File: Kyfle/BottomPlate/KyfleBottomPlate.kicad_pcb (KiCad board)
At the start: 2 copper layers, 161.3 x 139.1 mm, 52 parts, among them SW2 KEY_SWITCH, SW2 PRO MICRO

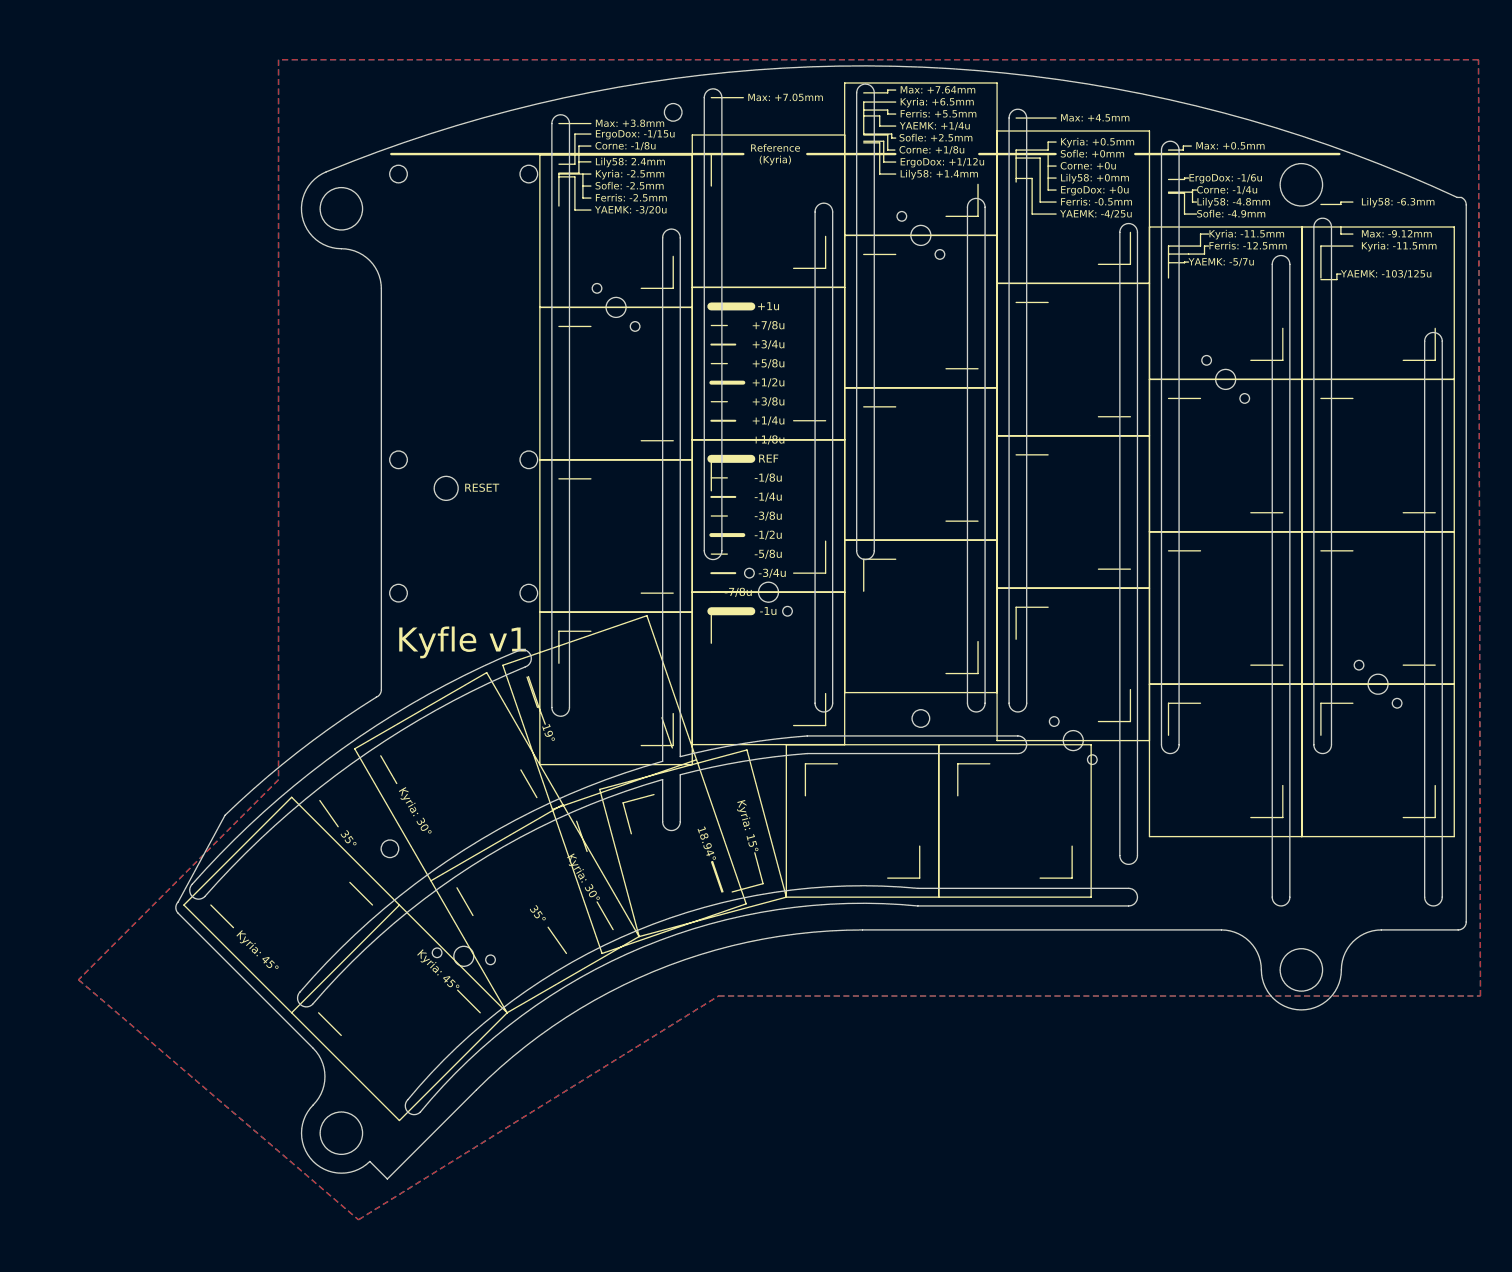
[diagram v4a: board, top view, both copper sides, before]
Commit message: Plates outlines finished
Redefined the various outlines of the plates based on the new constrains.
For the top dimension, I took the largest middle-finger stagerring I could find (Elephant42, at +9.5mm) and rounded it to 10mm max amplitude in the middle finger rail, and used that as reference for the position of the top arc (giving 3mm margin above that highest slot).
And defined the position of the rest from that.
Top left M% hole might need to be reviewed.
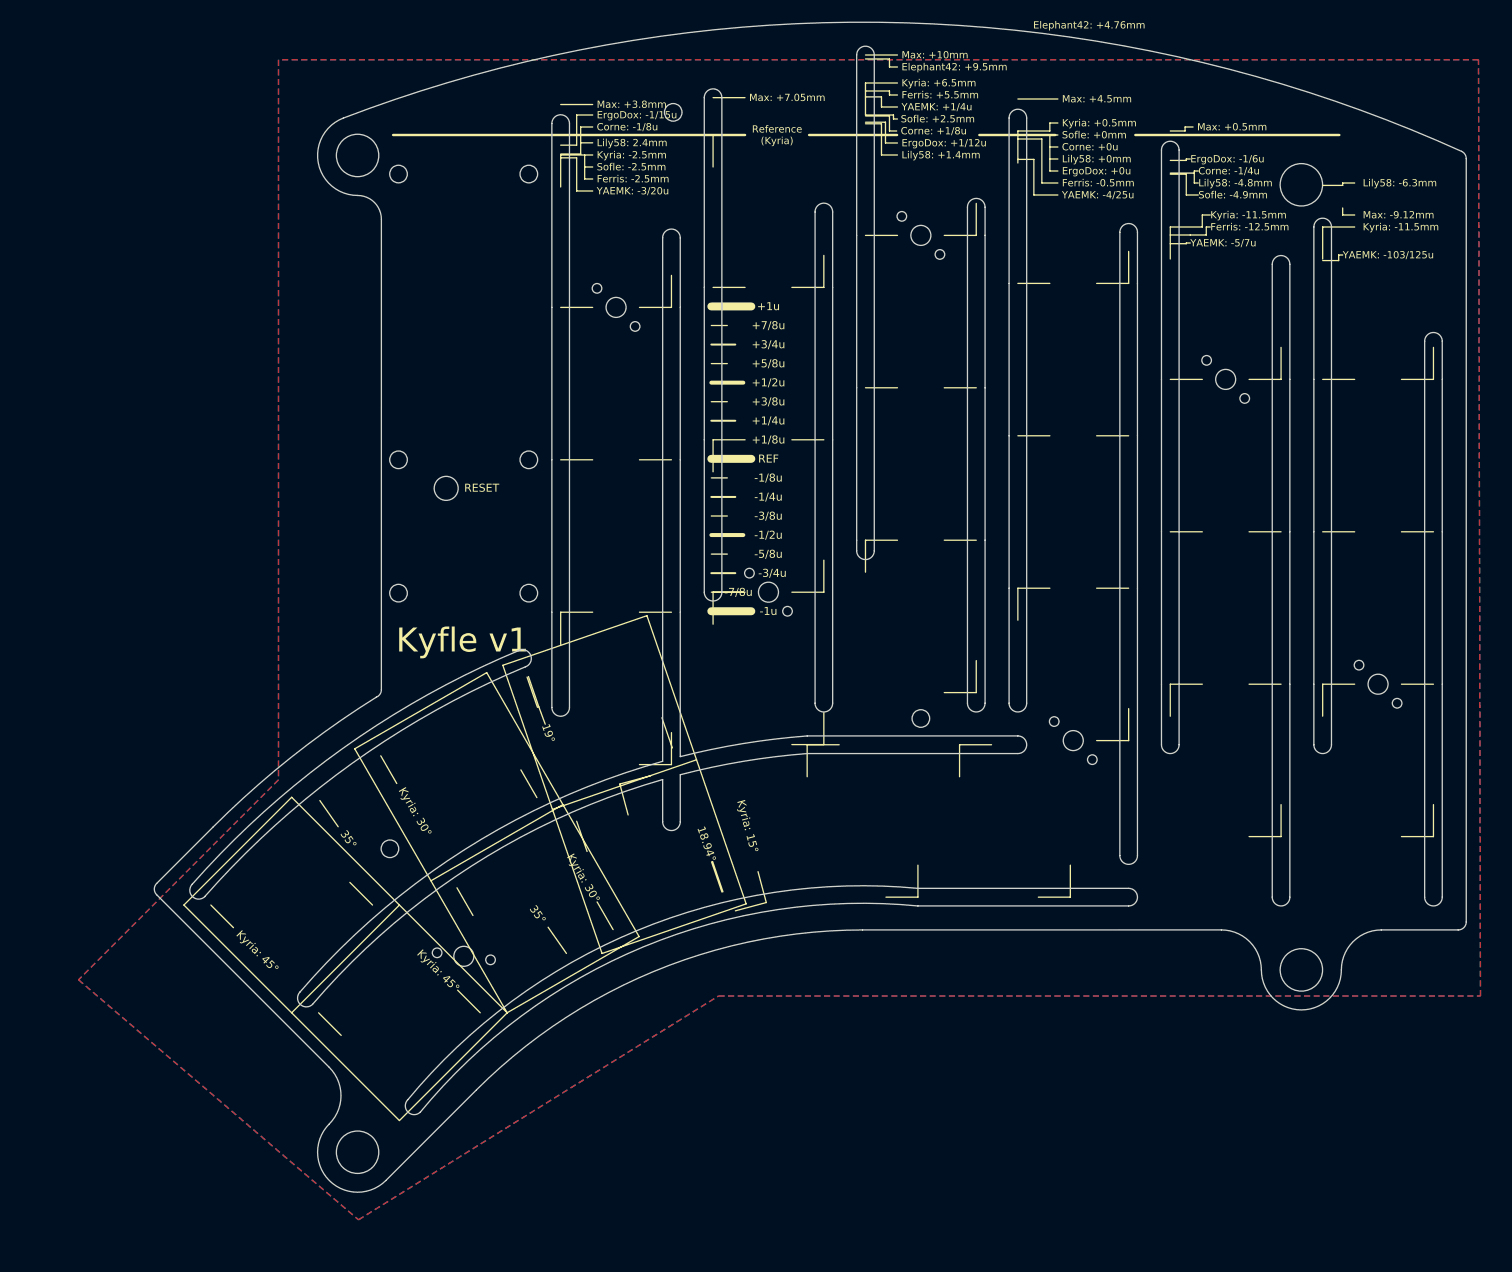
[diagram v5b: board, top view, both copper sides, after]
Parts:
- removed the REF** at (96.6, 157.1)
- added REF**: MountingHole_2.2mm_M2_ISO14580, Kyfle Footprints:M5_with_washer_and_board, F.Cu at (102.2, 163.1)
- moved Spacer 62.2 mm to (104.5, 44.9)
- moved REF** 6.97 mm to (98.6, 34.9)
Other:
- board size 161.3 x 139.1 mm -> 164 x 146.2 mm
- board text added: "Elephant42: +4.76mm"
- board text added: "Elephant42: +9.5mm"
- board text added: "Max: +10mm"
- board text removed: "Max: +7.64mm"

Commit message: Touch ups and small works
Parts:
- removed the REF** at (216.6, 38.6)
- removed the REF** at (216.6, 136.7)
- added REF**: MountingHole_2.2mm_M2_ISO14580, Kyfle Footprints:M5_with_washer_and_board, F.Cu at (237.2, 136.7)
- added REF**: MountingHole_2.2mm_M2_ISO14580, Kyfle Footprints:M5_with_washer, F.Cu at (232.2, 37.9)
- added Ref**: Val**, Kyfle Footprints:M2_with_washer, F.Cu at (124.0, 111.1)
- added SW2: KEY_SWITCH, Kyfle Footprints:CherryMX_Kyfle_v1_BottomPlate_2u, F.Cu at (123.1, 117.2)
- moved Spacer 25.2 mm to (118.5, 65.9), turned to 180 degrees
- moved SW2 12.4 mm to (180.8, 118.1)
- moved TH3 12.1 mm to (150.0, 27.4)
- moved SW2 9.52 mm to (150.0, 99.0)
- moved TH7 7.81 mm to (97.3, 116.0)
- moved TH7 1.26 mm to (169.1, 104.0)
- moved SW2 0.29 mm to (111.7, 134.8), turned to 352.5 degrees
- turned SW2 to 225 degrees
- turned SW2 to 210 degrees
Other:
- board size 164 x 146.2 mm -> 164 x 146.3 mm
- board text added: "Elephant42: +4.8mm"
- board text added: "Elephant42: -11.9mm"
- board text added: "Elephant42: -4.8mm"
- board text added: "Max: +0.7mm"
- board text added: "Max: +5.9mm"
- board text added: "Max: +6mm"
- board text added: "Max: +9mm"
- board text added: "Reference (Index)"
- board text removed: "Elephant42: +4.76mm"
- board text removed: "Max: +0.5mm"
- board text removed: "Max: +4.5mm"
- board text removed: "Max: -9.12mm"

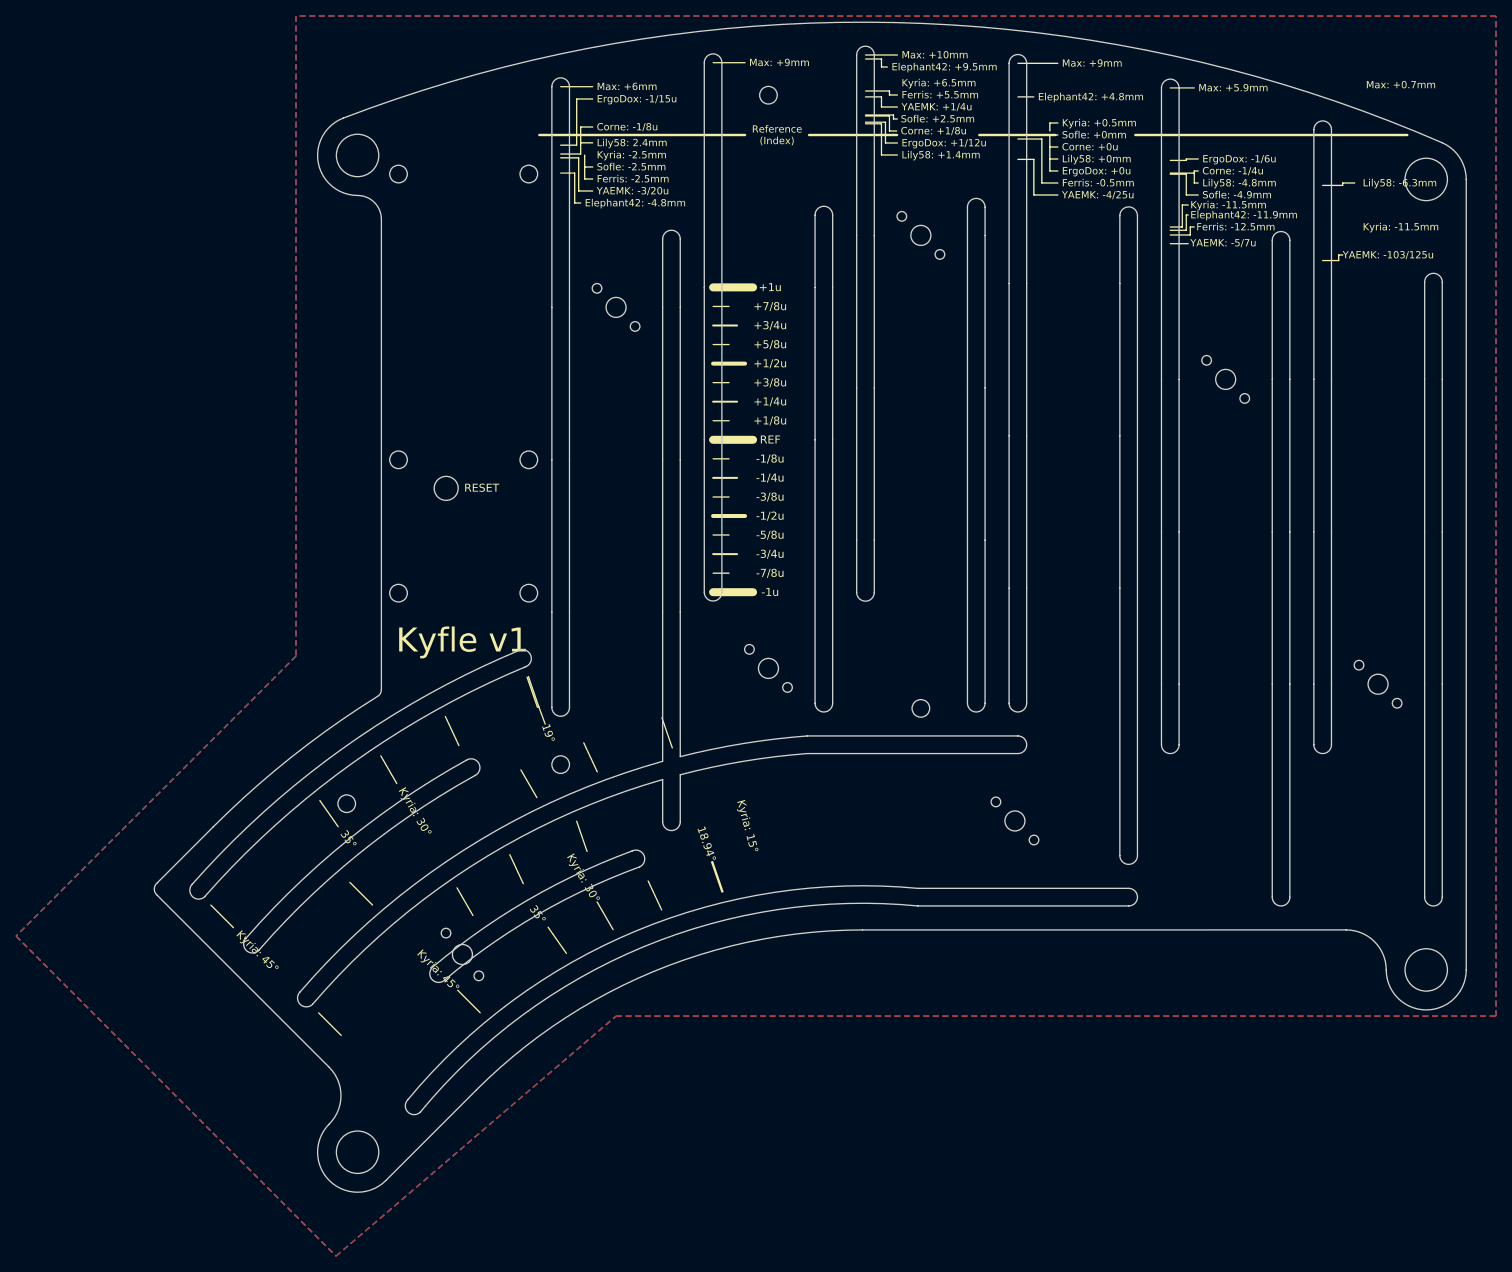
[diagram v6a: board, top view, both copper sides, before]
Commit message: Resized M2 slots and holes to 2mm instead of 2.2mm
After receiving M2 hardware, I noticed 2mm opening would provide a tighter and less wobbly fit than the typical M2 clearance of 2.2mm.

Also, finished the silkscreen of bottom plate, as well as M2 holes for encoders in top plate.
At this point, both top and bottom plate could be considered finished.
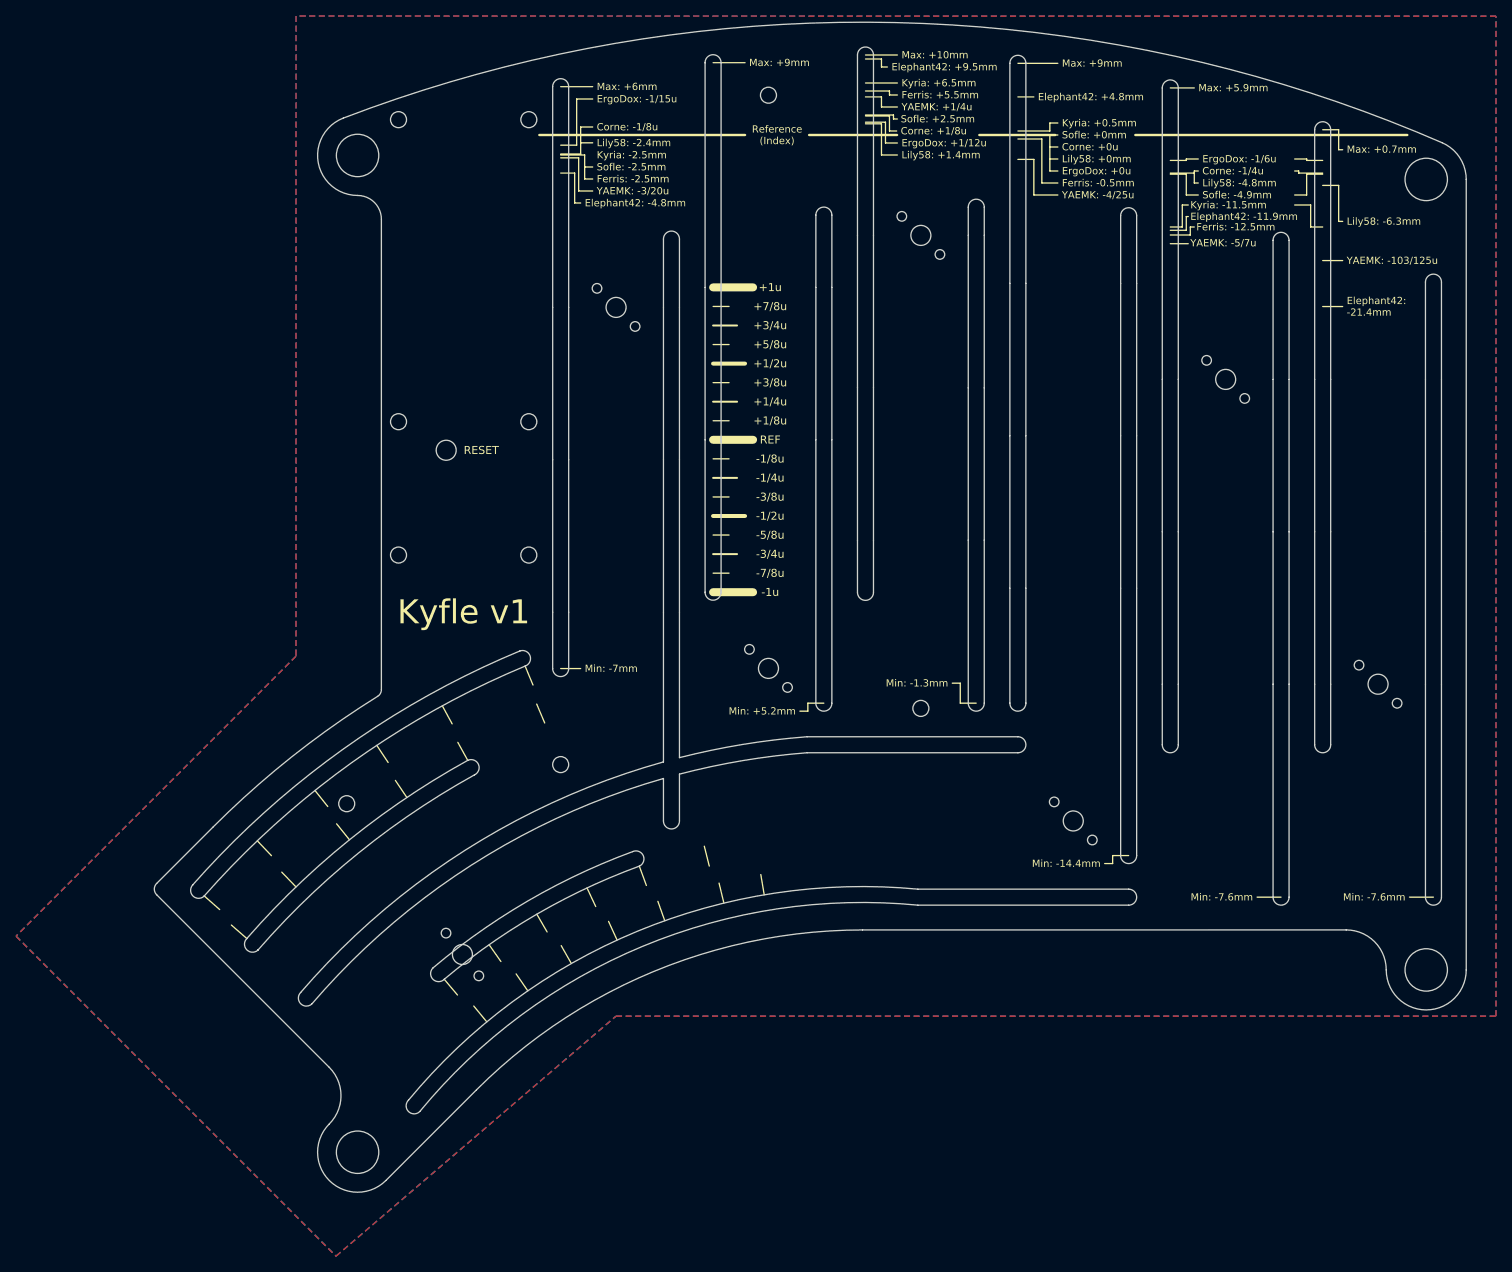
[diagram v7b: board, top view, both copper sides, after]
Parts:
- removed the REF** at (103.8, 37.3)
- removed the REF** at (120.0, 89.6)
- removed the REF** at (103.8, 89.6)
- removed the REF** at (103.8, 73.0)
- removed the REF** at (120.0, 73.0)
- removed the REF** at (120.0, 37.3)
- added SW2: 40°, Kyfle Footprints:CherryMX_Kyfle_v1_BottomPlate_2u, F.Cu at (103.0, 130.0)
- added SW2: 35°, Kyfle Footprints:CherryMX_Kyfle_v1_BottomPlate_2u, F.Cu at (109.3, 125.1)
- SW2: value KEY_SWITCH -> 15°; footprint Kyfle Footprints:CherryMX_Kyfle_v1_BottomPlate_1u_No_Rail -> Kyfle Footprints:CherryMX_Kyfle_v1_BottomPlate_1u_No_Rail_Angle_Silk
- SW2: value KEY_SWITCH -> 45°
- SW2: value KEY_SWITCH -> 25°
- SW2: value KEY_SWITCH -> 19°
- SW2: value KEY_SWITCH -> 30°
- moved Spacer 55.7 mm to (137.9, 118.1)
- moved SW2 7.29 mm to (188.1, 118.1)
- moved SW2 4.76 mm to (111.9, 58.7)
- turned SW2 to 45 degrees
- turned SW2 to 25 degrees
- turned SW2 to 30 degrees
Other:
- outline, holes or cut-outs redrawn
- rule pad_to_mask_clearance: 0.2 -> 0
- board text added: "Elephant42: -21.4mm"
- board text added: "Lily58: -2.4mm"
- board text added: "Min: +5.2mm"
- board text added: "Min: -1.3mm"
- board text added: "Min: -14.4mm"
- board text added: "Min: -7.6mm"
- board text added: "Min: -7mm"
- board text removed: "18.94°"
- board text removed: "19°"
- board text removed: "35°"
- board text removed: "Kyria: 15°"
- board text removed: "Kyria: 30°"
- board text removed: "Kyria: 45°"
- board text removed: "Lily58: 2.4mm"
- board text removed: "Max: +3.8mm"
- board text removed: "Max: +7.05mm"
- board text removed: "RESET"
- board text removed: "Reference (Kyria)"
